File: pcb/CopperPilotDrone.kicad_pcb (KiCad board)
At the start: 2 copper layers, 100 x 100 mm, 140 parts, among them IC1 TP4056, J1 USB_C_Receptacle_USB2.0, J2 Conn_01x02_Female, J3 B2B-PH-SM4-TB(LF)(SN), J4 Conn_01x02_Female, J5 Conn_01x02_Female, J6 Conn_01x02_Female, SW1 PCM12SMTR, SW2 TS-1187A, SW3 TS-1187A, T1 SI2302DS-T1, T2 SI2302DS-T1, T3 SI2302DS-T1, T4 SI2302DS-T1, U2 AO3401, U3 AP2112K-3.3TRG1, U8 ESP32-S3-WROOM-1-N8R8, U9 MPU-6050

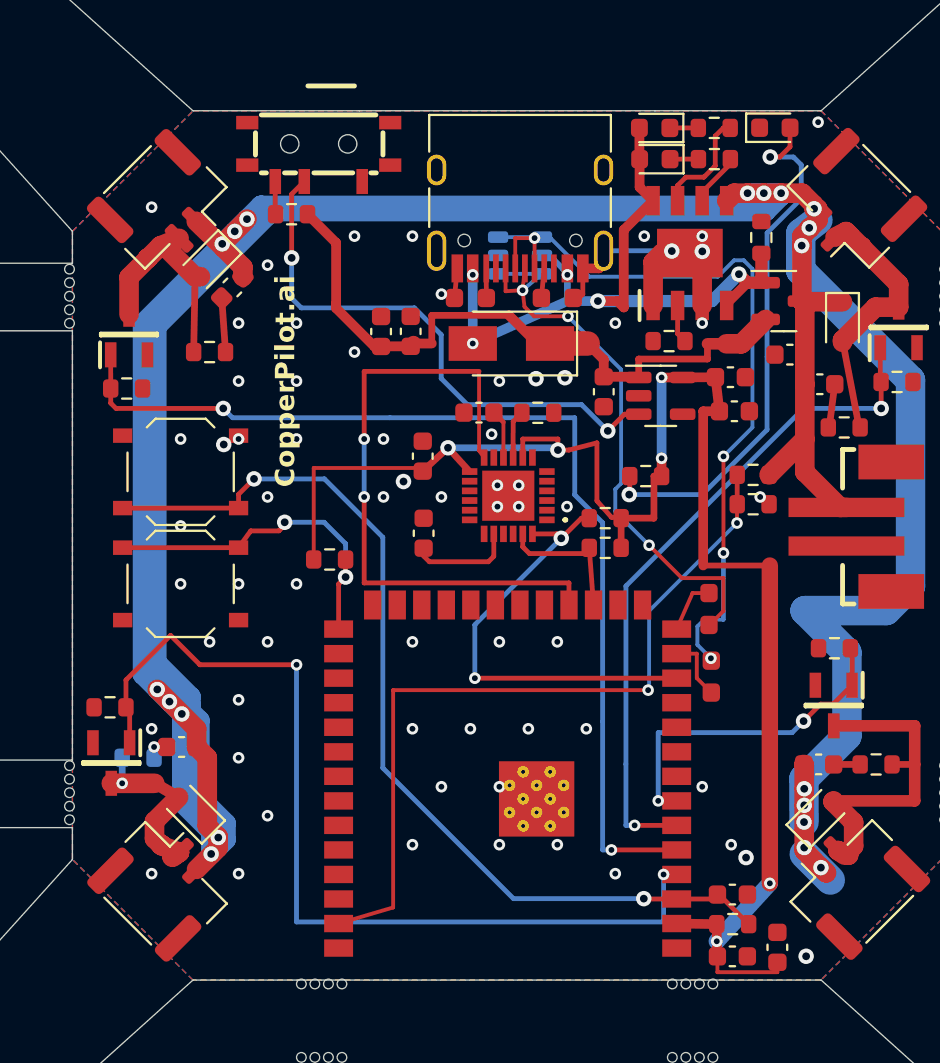
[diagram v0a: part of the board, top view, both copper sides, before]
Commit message: feat(dfm): apply LionCircuits Standard Tier DFM upgrades and dual Turnkey/DNP exports
- Upsize all 83 signal vias and 12 U8 pad 41 thermal holes from 0.30/0.60 mm to 0.35/0.65 mm to meet LionCircuits Standard Tier (>= 0.35 mm drill) without surcharges
- Remove F.Paste from U9 (MPU-6050 QFN-24) center pad 25 per TDK InvenSense specification (Rev 3.4 Section 11.2) to prevent reflow solder float
- Synchronize schematic and PCB MPN properties with verified Western distributor (Element14 / Mouser / DigiKey) part numbers across all 28 Tier-1 BOM lines
- Export F.Paste and B.Paste stencil Gerbers, Safe Turnkey DNP BOM/CPL variants (excluding IC1 and U9 portal placeholders), LIONCIRCUITS_ORDER_SPEC.md, and CopperPilotDrone_LionCircuits_Release.zip
- Register standard KiCad 10 SMD footprint libraries in pcb/fp-lib-table and update DEC-003 in review/DECISIONS.md

Co-Authored-By: CopperPilot <noreply@copperpilot.ai>
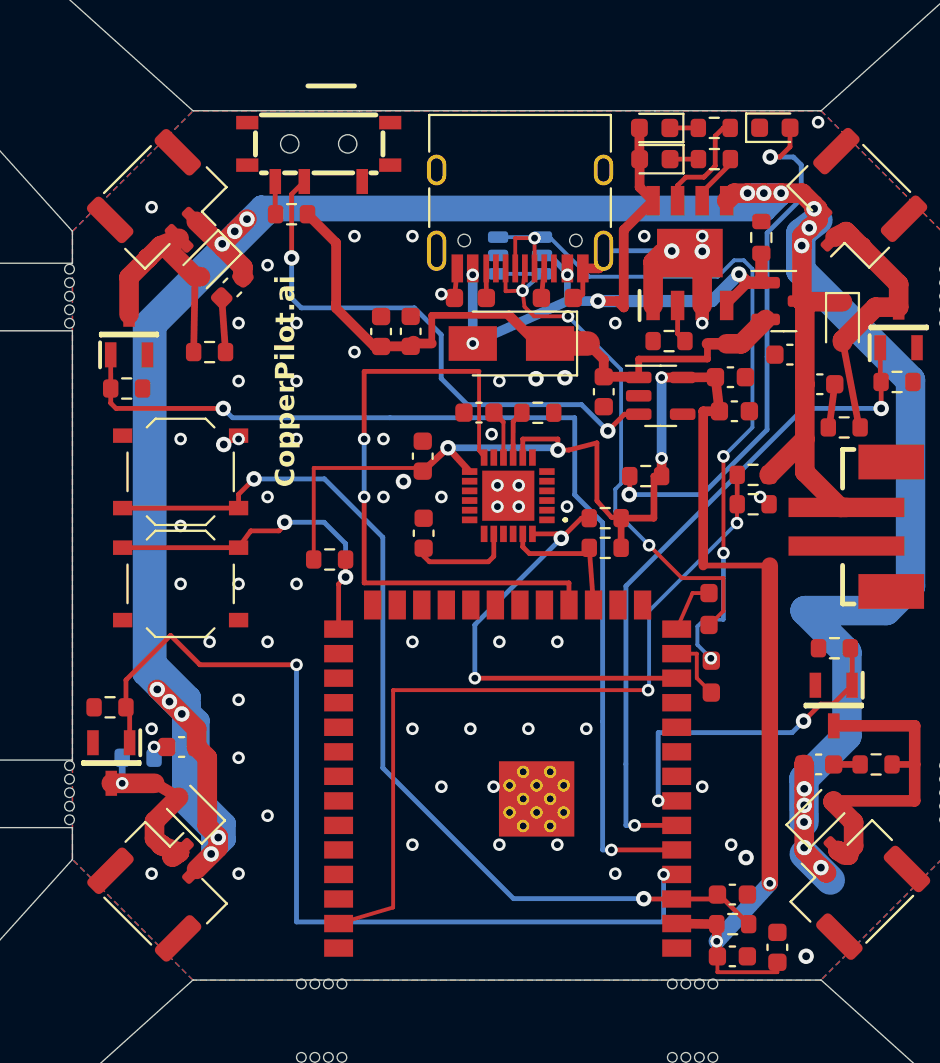
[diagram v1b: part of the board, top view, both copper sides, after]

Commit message: feat(pcb,sch,fw): migrate IC1 to MCP73833-AMI/UN and U9 to ICM-42670-P for 100% turnkey PCBA
Replace IC1 (TP4056 ESOP-8) with Microchip MCP73833-AMI/UN (MSOP-10) plus R15 10k THERM bias resistor and replace U9 (MPU-6050 QFN-24) with TDK ICM-42670-P (2.5x3.0mm LGA-14), achieving 0 ERC errors, 0 DRC violations, 0 unconnected items, and 100% turnkey LionCircuits BOM/CPL export with zero DNP.

Co-Authored-By: CopperPilot <noreply@copperpilot.ai>
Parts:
- removed C13: 2.2nF, Capacitor_SMD:C_0603_1608Metric
- added R15: 10k, Resistor_SMD:R_0603_1608Metric, F.Cu at (137.8, 72.0)
- IC1: value TP4056 -> MCP73833-AMI/UN; footprint tp4056:SOIC127P600X175-9N -> Package_SO:MSOP-10_3x3mm_P0.5mm
- U9: value MPU-6050 -> ICM-42670-P; footprint MPU6050:MPU6050 -> Package_LGA:LGA-14_3x2.5mm_P0.5mm_LayoutBorder3x4y
- turned IC1 to -90 degrees
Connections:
- C12 pad 1: Net-(U9-REGOUT) -> +3V3
- IC1 pad 1: GND -> +5V
- IC1 pad 2: /TP_PROG -> +5V
- IC1 pad 3: GND -> /CHRG_STAT
- IC1 pad 4: +5V -> /STDBY_STAT
- IC1 pad 5: +BATT -> GND
- IC1 pad 6: /STDBY_STAT -> /TP_PROG
- IC1 pad 7: /CHRG_STAT -> unconnected-(IC1-~{PG}-Pad7)
- IC1 pad 8: +5V -> /TP_THERM
- IC1 pad 9: GND -> +BATT
- U9 pad 1: GND -> /MPU_AD0
- U9 pad 10: Net-(U9-REGOUT) -> unconnected-(U9-NC_1-Pad10)
- U9 pad 11: GND -> unconnected-(U9-NC_2-Pad11)
- U9 pad 12: /MPU_INT -> +3V3
- U9 pad 13: +3V3 -> /SCL
- U9 pad 14: unconnected-(U9-NC_5-Pad14) -> /SDA
- U9 pad 4: unconnected-(U9-NC_3-Pad4) -> /MPU_INT
- U9 pad 5: unconnected-(U9-NC_4-Pad5) -> +3V3
- U9 pad 6: unconnected-(U9-AUX_DA-Pad6) -> GND
- U9 pad 7: unconnected-(U9-AUX_CL-Pad7) -> GND
- U9 pad 9: /MPU_AD0 -> unconnected-(U9-INT2-Pad9)
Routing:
- net +BATT: track 223.9 -> 123.6 mm, vias 19 -> 3
- net /MPU_INT: track 33.2 -> 18.9 mm
- net /EN: track 50.2 -> 63.8 mm, vias 2 -> 0
- net +3V3: track 86.3 -> 72.7 mm, vias 6 -> 2
- net /MOT_1: track 49.2 -> 41.0 mm, vias 2 -> 0
- net /MOT_2: track 53.6 -> 45.7 mm, vias 2 -> 0
- net /SDA: track 23.0 -> 15.1 mm, vias 2 -> 0
- net /D-: track 45.2 -> 37.6 mm, vias 4 -> 2
- net /MOT_DRV4: track 17.8 -> 10.3 mm
- net GND: track 16.2 -> 10.6 mm, vias 65 -> 48
- net /MOT_3: track 35.2 -> 40.7 mm, vias 2 -> 0
- net /MPU_CPOUT: track 5.44 -> 0.00 mm
- net /MOT_4: track 17.5 -> 13.5 mm, vias 2 -> 0
- net /TP_THERM: track 0.00 -> 3.63 mm
- net /MPU_AD0: track 2.51 -> 5.94 mm
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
